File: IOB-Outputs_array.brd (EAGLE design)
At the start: 106.7 x 104.1 mm, 112 parts

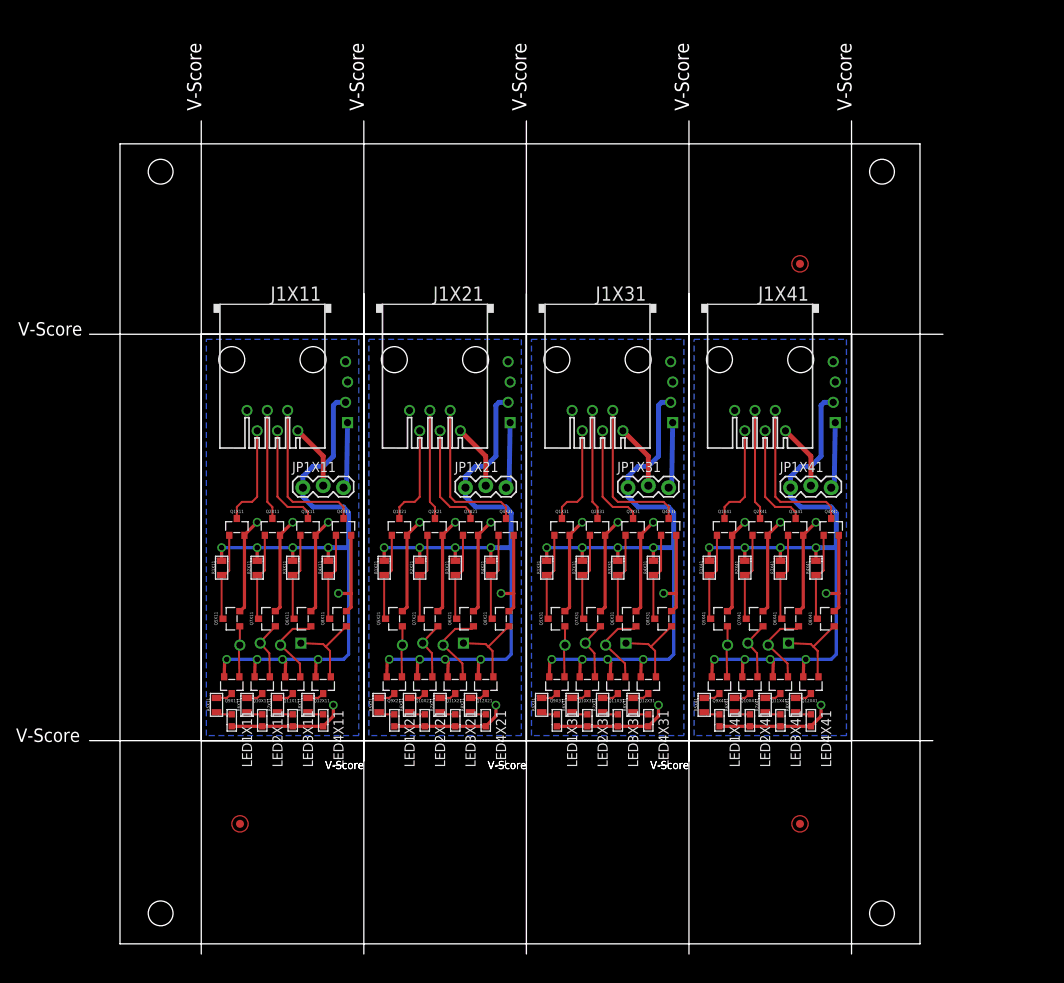
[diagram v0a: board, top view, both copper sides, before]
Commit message: updated to new IOB design
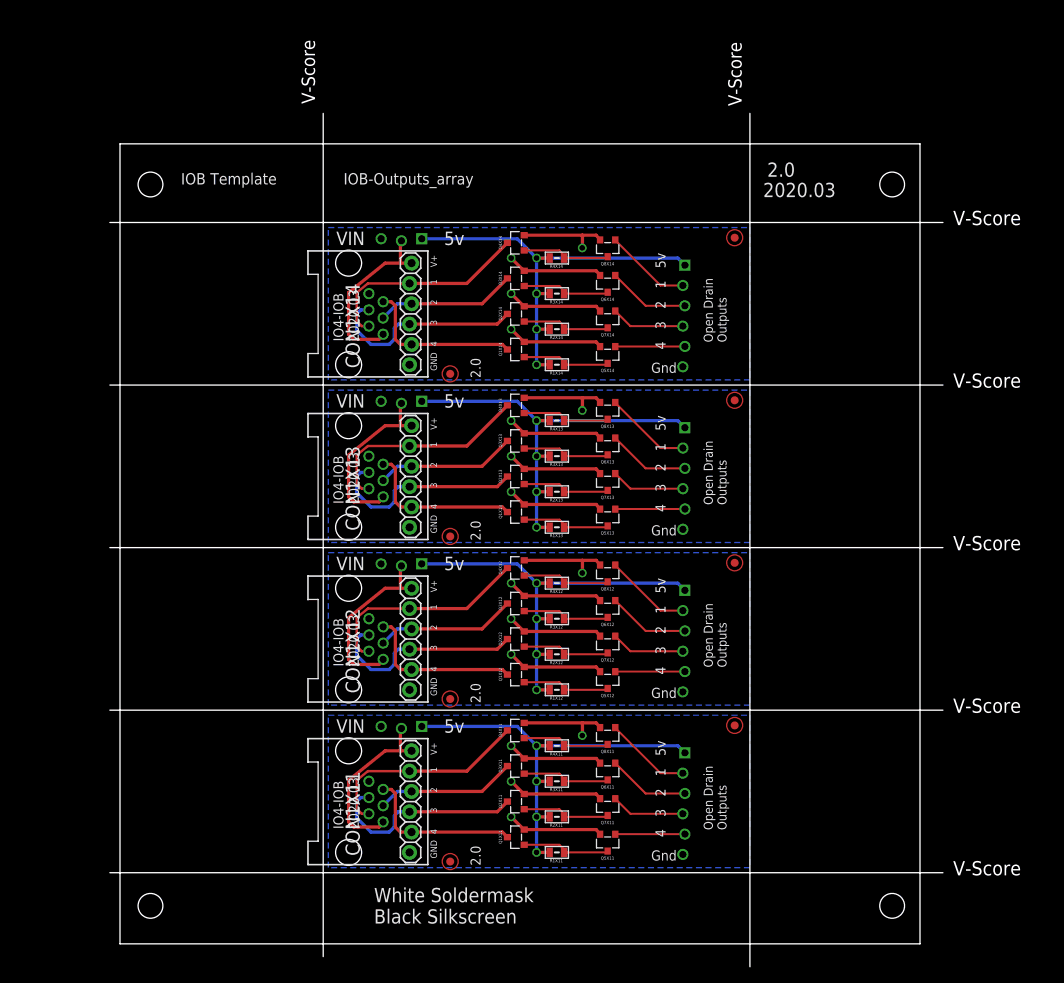
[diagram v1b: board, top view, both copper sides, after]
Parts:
- removed IOBX11, IOBX21, IOBX31, IOBX41: (no value), SPCoast:IO4-IOB
- removed J1X11, J1X21, J1X31, J1X41: (no value), SPCoast:RJ25-PANEL
- removed JP1X11, JP1X21, JP1X31, JP1X41: (no value), SPCoast:1X03
- removed LED1X11, LED1X21, LED1X31, LED1X41, LED2X11, LED2X21, LED2X31, LED2X41, LED3X11, LED3X21, LED3X31, LED3X41, LED4X11, LED4X21, LED4X31, LED4X41: (no value), SPCoast:0603-LED
- removed Q10X11, Q10X21, Q10X31, Q10X41, Q11X11, Q11X21, Q11X31, Q11X41, Q12X11, Q12X21, Q12X31, Q12X41, Q1X21, Q1X31, Q1X41, Q2X21, Q2X31, Q2X41, Q3X21, Q3X31, Q3X41, Q4X21, Q4X31, Q4X41, Q5X21, Q5X31, Q5X41, Q6X21, Q6X31, Q6X41, Q7X21, Q7X31, Q7X41, Q8X21, Q8X31, Q8X41, Q9X11, Q9X21, Q9X31, Q9X41: (no value), SPCoast:SOT23-3
- removed R1X21, R1X31, R1X41, R2X21, R2X31, R2X41, R3X21, R3X31, R3X41, R4X21, R4X31, R4X41, R5X11, R5X21, R5X31, R5X41, R6X11, R6X21, R6X31, R6X41, R7X11, R7X21, R7X31, R7X41, R8X11, R8X21, R8X31, R8X41: (no value), SPCoast:0805-RES
- removed R8X1: (no value), SPCoast:BOARD-DINRAIL-3.17IN-4X-IOB
- removed R8X2, R8X3, R8X4: (no value), SPCoast:FIDUCIAL_1MM
- added CON1X11, CON1X12, CON1X13, CON1X14: (no value), SPCoast:RJ24-INVERTED-PINS
- added FID1X11, FID1X12, FID1X13, FID1X14, FID2X11, FID2X12, FID2X13, FID2X14: (no value), SPCoast:FIDUCIAL_1MM
- added Q1X12, Q1X13, Q1X14, Q2X12, Q2X13, Q2X14, Q3X12, Q3X13, Q3X14, Q4X12, Q4X13, Q4X14, Q5X12, Q5X13, Q5X14, Q6X12, Q6X13, Q6X14, Q7X12, Q7X13, Q7X14, Q8X12, Q8X13, Q8X14: (no value), SPCoast:SOT23-3
- added R1X12, R1X13, R1X14, R2X12, R2X13, R2X14, R3X12, R3X13, R3X14, R4X12, R4X13, R4X14: (no value), SPCoast:0805-RES
- added U$1X1: (no value), SPCoast:BOARD-DINRAIL-3.17IN-H4X-IOB
- added U$1X11, U$1X12, U$1X13, U$1X14: (no value), SPCoast:IO4-IOB
- moved R1X11 55.0 mm to (54.6, 11.4), turned to 180 degrees
- moved Q5X11 54.7 mm to (61.0, 12.7), turned to 180 degrees
- moved Q1X11 52.2 mm to (49.5, 13.3), turned to 90 degrees
- moved R2X11 48.7 mm to (54.6, 15.9), turned to 180 degrees
- moved Q7X11 48.6 mm to (61.0, 17.1), turned to 180 degrees
- moved Q2X11 45.9 mm to (49.5, 17.8), turned to 90 degrees
- moved Q6X11 42.6 mm to (61.0, 21.6), turned to 180 degrees
- moved R3X11 42.4 mm to (54.6, 20.3), turned to 180 degrees
- moved Q3X11 39.6 mm to (49.5, 22.2), turned to 90 degrees
- moved Q8X11 36.7 mm to (61.0, 26.0), turned to 180 degrees
- moved R4X11 36.2 mm to (54.6, 24.8), turned to 180 degrees
- moved Q4X11 33.3 mm to (49.5, 26.7), turned to 90 degrees
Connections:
- removed net GNDX21: IOBX21.G@1, IOBX21.G@2, J1X21.6, LED1X21.C, LED2X21.C, LED3X21.C, LED4X21.C, Q1X21.2, Q2X21.2, Q3X21.2, Q4X21.2, Q5X21.2, Q6X21.2, Q7X21.2, Q8X21.2
- removed net GNDX31: IOBX31.G@1, IOBX31.G@2, J1X31.6, LED1X31.C, LED2X31.C, LED3X31.C, LED4X31.C, Q1X31.2, Q2X31.2, Q3X31.2, Q4X31.2, Q5X31.2, Q6X31.2, Q7X31.2, Q8X31.2
- removed net GNDX41: IOBX41.G@1, IOBX41.G@2, J1X41.6, LED1X41.C, LED2X41.C, LED3X41.C, LED4X41.C, Q1X41.2, Q2X41.2, Q3X41.2, Q4X41.2, Q5X41.2, Q6X41.2, Q7X41.2, Q8X41.2
- removed net IO1X21: J1X21.2, Q4X21.3
- removed net IO1X31: J1X31.2, Q4X31.3
- removed net IO1X41: J1X41.2, Q4X41.3
- removed net IO2X21: J1X21.3, Q3X21.3
- removed net IO2X31: J1X31.3, Q3X31.3
- removed net IO2X41: J1X41.3, Q3X41.3
- removed net IO3X21: J1X21.4, Q2X21.3
- removed net IO3X31: J1X31.4, Q2X31.3
- removed net IO3X41: J1X41.4, Q2X41.3
- removed net IO4X21: J1X21.5, Q1X21.3
- removed net IO4X31: J1X31.5, Q1X31.3
- removed net IO4X41: J1X41.5, Q1X41.3
- removed net N$11X11: Q12X11.3, R8X11.2
- removed net N$11X21: Q12X21.3, R8X21.2
- removed net N$11X31: Q12X31.3, R8X31.2
- removed net N$11X41: Q12X41.3, R8X41.2
- removed net N$1X21: Q4X21.1, Q8X21.3, R4X21.1
- removed net N$1X31: Q4X31.1, Q8X31.3, R4X31.1
- removed net N$1X41: Q4X41.1, Q8X41.3, R4X41.1
- removed net N$2X11: LED4X11.A, R8X11.1
- removed net N$2X21: LED4X21.A, R8X21.1
- removed net N$2X31: LED4X31.A, R8X31.1
- removed net N$2X41: LED4X41.A, R8X41.1
- removed net N$30X11: Q11X11.3, R7X11.2
- removed net N$30X21: Q11X21.3, R7X21.2
- removed net N$30X31: Q11X31.3, R7X31.2
- removed net N$30X41: Q11X41.3, R7X41.2
- removed net N$31X11: Q10X11.3, R6X11.2
- removed net N$31X21: Q10X21.3, R6X21.2
- removed net N$31X31: Q10X31.3, R6X31.2
- removed net N$31X41: Q10X41.3, R6X41.2
- removed net N$32X11: Q9X11.3, R5X11.2
- removed net N$32X21: Q9X21.3, R5X21.2
- removed net N$32X31: Q9X31.3, R5X31.2
- removed net N$32X41: Q9X41.3, R5X41.2
- removed net N$3X11: LED3X11.A, R7X11.1
- removed net N$3X21: LED3X21.A, R7X21.1
- removed net N$3X31: LED3X31.A, R7X31.1
- removed net N$3X41: LED3X41.A, R7X41.1
- removed net N$4X11: LED2X11.A, R6X11.1
- removed net N$4X21: LED2X21.A, R6X21.1
- removed net N$4X31: LED2X31.A, R6X31.1
- removed net N$4X41: LED2X41.A, R6X41.1
- removed net N$5X11: LED1X11.A, R5X11.1
- removed net N$5X21: LED1X21.A, R5X21.1
- removed net N$5X31: LED1X31.A, R5X31.1
- removed net N$5X41: LED1X41.A, R5X41.1
- removed net N$6X21: Q3X21.1, Q6X21.3, R3X21.1
- removed net N$6X31: Q3X31.1, Q6X31.3, R3X31.1
- removed net N$6X41: Q3X41.1, Q6X41.3, R3X41.1
- removed net N$7X21: Q2X21.1, Q7X21.3, R2X21.1
- removed net N$7X31: Q2X31.1, Q7X31.3, R2X31.1
- removed net N$7X41: Q2X41.1, Q7X41.3, R2X41.1
- removed net N$8X21: Q1X21.1, Q5X21.3, R1X21.1
- removed net N$8X31: Q1X31.1, Q5X31.3, R1X31.1
- removed net N$8X41: Q1X41.1, Q5X41.3, R1X41.1
- removed net P1X21: IOBX21.P1, Q12X21.1, Q8X21.1
- removed net P1X31: IOBX31.P1, Q12X31.1, Q8X31.1
- removed net P1X41: IOBX41.P1, Q12X41.1, Q8X41.1
- removed net P2X21: IOBX21.P2, Q11X21.1, Q6X21.1
- removed net P2X31: IOBX31.P2, Q11X31.1, Q6X31.1
- removed net P2X41: IOBX41.P2, Q11X41.1, Q6X41.1
- removed net P3X21: IOBX21.P3, Q10X21.1, Q7X21.1
- removed net P3X31: IOBX31.P3, Q10X31.1, Q7X31.1
- removed net P3X41: IOBX41.P3, Q10X41.1, Q7X41.1
- removed net P4X21: IOBX21.P4, Q5X21.1, Q9X21.1
- removed net P4X31: IOBX31.P4, Q5X31.1, Q9X31.1
- removed net P4X41: IOBX41.P4, Q5X41.1, Q9X41.1
- removed net VCCIOX11: J1X11.1, JP1X11.2
- removed net VCCIOX21: J1X21.1, JP1X21.2
- removed net VCCIOX31: J1X31.1, JP1X31.2
- removed net VCCIOX41: J1X41.1, JP1X41.2
- removed net VCCX21: IOBX21.V5, JP1X21.1, Q10X21.2, Q11X21.2, Q12X21.2, Q9X21.2, R1X21.2, R2X21.2, R3X21.2, R4X21.2
- removed net VCCX31: IOBX31.V5, JP1X31.1, Q10X31.2, Q11X31.2, Q12X31.2, Q9X31.2, R1X31.2, R2X31.2, R3X31.2, R4X31.2
- removed net VCCX41: IOBX41.V5, JP1X41.1, Q10X41.2, Q11X41.2, Q12X41.2, Q9X41.2, R1X41.2, R2X41.2, R3X41.2, R4X41.2
- removed net VINX21: IOBX21.V+, JP1X21.3
- removed net VINX31: IOBX31.V+, JP1X31.3
- removed net VINX41: IOBX41.V+, JP1X41.3
- new net GNDX12: CON1X12.6, CON1X12.6@1, Q1X12.2, Q2X12.2, Q3X12.2, Q4X12.2, Q5X12.2, Q6X12.2, Q7X12.2, Q8X12.2, U$1X12.G@3
- new net GNDX13: CON1X13.6, CON1X13.6@1, Q1X13.2, Q2X13.2, Q3X13.2, Q4X13.2, Q5X13.2, Q6X13.2, Q7X13.2, Q8X13.2, U$1X13.G@3
- new net GNDX14: CON1X14.6, CON1X14.6@1, Q1X14.2, Q2X14.2, Q3X14.2, Q4X14.2, Q5X14.2, Q6X14.2, Q7X14.2, Q8X14.2, U$1X14.G@3
- new net IO1X12: CON1X12.2, CON1X12.2@1, Q4X12.3
- new net IO1X13: CON1X13.2, CON1X13.2@1, Q4X13.3
- new net IO1X14: CON1X14.2, CON1X14.2@1, Q4X14.3
- new net IO2X12: CON1X12.3, CON1X12.3@1, Q3X12.3
- new net IO2X13: CON1X13.3, CON1X13.3@1, Q3X13.3
- new net IO2X14: CON1X14.3, CON1X14.3@1, Q3X14.3
- new net IO3X12: CON1X12.4, CON1X12.4@1, Q2X12.3
- new net IO3X13: CON1X13.4, CON1X13.4@1, Q2X13.3
- new net IO3X14: CON1X14.4, CON1X14.4@1, Q2X14.3
- new net IO4X12: CON1X12.5, CON1X12.5@1, Q1X12.3
- new net IO4X13: CON1X13.5, CON1X13.5@1, Q1X13.3
- new net IO4X14: CON1X14.5, CON1X14.5@1, Q1X14.3
- new net N$1X12: Q4X12.1, Q8X12.3, R4X12.1
- new net N$1X13: Q4X13.1, Q8X13.3, R4X13.1
- new net N$1X14: Q4X14.1, Q8X14.3, R4X14.1
- new net N$6X12: Q3X12.1, Q6X12.3, R3X12.1
- new net N$6X13: Q3X13.1, Q6X13.3, R3X13.1
- new net N$6X14: Q3X14.1, Q6X14.3, R3X14.1
- new net N$7X12: Q2X12.1, Q7X12.3, R2X12.1
- new net N$7X13: Q2X13.1, Q7X13.3, R2X13.1
- new net N$7X14: Q2X14.1, Q7X14.3, R2X14.1
- new net N$8X12: Q1X12.1, Q5X12.3, R1X12.1
- new net N$8X13: Q1X13.1, Q5X13.3, R1X13.1
- new net N$8X14: Q1X14.1, Q5X14.3, R1X14.1
- new net P1X12: Q8X12.1, U$1X12.P1
- new net P1X13: Q8X13.1, U$1X13.P1
- new net P1X14: Q8X14.1, U$1X14.P1
- new net P2X12: Q6X12.1, U$1X12.P2
- new net P2X13: Q6X13.1, U$1X13.P2
- new net P2X14: Q6X14.1, U$1X14.P2
- new net P3X12: Q7X12.1, U$1X12.P3
- new net P3X13: Q7X13.1, U$1X13.P3
- new net P3X14: Q7X14.1, U$1X14.P3
- new net P4X12: Q5X12.1, U$1X12.P4
- new net P4X13: Q5X13.1, U$1X13.P4
- new net P4X14: Q5X14.1, U$1X14.P4
- new net VCCX12: R1X12.2, R2X12.2, R3X12.2, R4X12.2, U$1X12.V5, U$1X12.V5@1
- new net VCCX13: R1X13.2, R2X13.2, R3X13.2, R4X13.2, U$1X13.V5, U$1X13.V5@1
- new net VCCX14: R1X14.2, R2X14.2, R3X14.2, R4X14.2, U$1X14.V5, U$1X14.V5@1
- new net VINX12: U$1X12.V+
- new net VINX13: U$1X13.V+
- new net VINX14: U$1X14.V+
- new net VOUTX11: CON1X11.1, CON1X11.1@1, U$1X11.VOUT
- new net VOUTX12: CON1X12.1, CON1X12.1@1, U$1X12.VOUT
- new net VOUTX13: CON1X13.1, CON1X13.1@1, U$1X13.VOUT
- new net VOUTX14: CON1X14.1, CON1X14.1@1, U$1X14.VOUT
- net GNDX11: now also CON1X11.6, CON1X11.6@1, U$1X11.G@3; no longer IOBX11.G@1, IOBX11.G@2, J1X11.6, LED1X11.C, LED2X11.C, LED3X11.C, LED4X11.C
- net IO1X11: now also CON1X11.2, CON1X11.2@1; no longer J1X11.2
- net IO2X11: now also CON1X11.3, CON1X11.3@1; no longer J1X11.3
- net IO3X11: now also CON1X11.4, CON1X11.4@1; no longer J1X11.4
- net IO4X11: now also CON1X11.5, CON1X11.5@1; no longer J1X11.5
- net P1X11: now also U$1X11.P1; no longer IOBX11.P1, Q12X11.1
- net P2X11: now also U$1X11.P2; no longer IOBX11.P2, Q11X11.1
- net P3X11: now also U$1X11.P3; no longer IOBX11.P3, Q10X11.1
- net P4X11: now also U$1X11.P4; no longer IOBX11.P4, Q9X11.1
- net VCCX11: now also U$1X11.V5, U$1X11.V5@1; no longer IOBX11.V5, JP1X11.1, Q10X11.2, Q11X11.2, Q12X11.2, Q9X11.2
- net VINX11: now also U$1X11.V+; no longer IOBX11.V+, JP1X11.3
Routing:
- net VCCX41: track 86.8 -> 0.00 mm, vias 8 -> 0
- net VCCX31: track 86.8 -> 0.00 mm, vias 8 -> 0
- net VCCX21: track 86.8 -> 0.00 mm, vias 8 -> 0
- net GNDX31: track 62.1 -> 0.00 mm, vias 5 -> 0
- net GNDX21: track 62.1 -> 0.00 mm, vias 5 -> 0
- net GNDX41: track 62.1 -> 0.00 mm, vias 5 -> 0
- net VCCX12: track 0.00 -> 54.2 mm, vias 0 -> 4
- net VCCX14: track 0.00 -> 54.2 mm, vias 0 -> 4
- net VCCX13: track 0.00 -> 54.2 mm, vias 0 -> 4
- net GNDX13: track 0.00 -> 47.5 mm, vias 0 -> 4
- net GNDX12: track 0.00 -> 47.5 mm, vias 0 -> 4
- net GNDX14: track 0.00 -> 47.5 mm, vias 0 -> 4
- net VCCX11: track 86.8 -> 54.2 mm, vias 8 -> 4
- net IO1X14: track 0.00 -> 26.7 mm
- net IO1X13: track 0.00 -> 26.7 mm
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- added copper zone on layer 16, net GNDX12
- added copper zone on layer 16, net GNDX13
- added copper zone on layer 16, net GNDX14
- removed copper zone on layer 16, net GNDX21
- removed copper zone on layer 16, net GNDX31
- removed copper zone on layer 16, net GNDX41
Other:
- board size 106.7 x 104.1 mm -> 104.1 x 106.7 mm
- board text added: "2020.03"
- board text added: "CON1"
- board text added: "White Soldermask Black Silkscreen"
- board text removed: "(15,15)"
- board text removed: "(15,85)"
- board text removed: "(85,85)"
- board text removed: "1"
- board text removed: "2"
- board text removed: "2019-11"
- board text removed: "3"
- board text removed: "4"
- board text removed: "5V"
- board text removed: "5v"
- board text removed: "IO Interface"
- board text removed: "IO4 Power"
- board text removed: "J1"
- board text removed: "JP1"
- board text removed: "Made in the PCR, Coast Div, NMRA"
- board text removed: "Model Railroading is Fun!"
- board text removed: "P1"
- board text removed: "P2"
- board text removed: "P3"
- board text removed: "P4"
- board text removed: "Q10"
- board text removed: "Q11"
- board text removed: "Q12"
- board text removed: "Q9"
- board text removed: "Quad OpenDrain Output"
- board text removed: "R5"
- board text removed: "R6"
- board text removed: "R7"
- board text removed: "R8"
- board text removed: "V-Score"
- board text removed: "V2.0"
- board text removed: "VIN"
- board text removed: "Vin"
- board text removed: "White Soldermask, Black Silkscreen"

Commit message: bump version
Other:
- board text added: "3.0"
- board text added: "v3.0"
- board text removed: "2.0"
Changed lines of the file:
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@@
 <plain>
 <text x="27.94" y="14.351" size="1.27" layer="21" font="vector" rot="R90">IO4-IOB</text>
-<text x="45.085" y="9.779" size="1.27" layer="21" font="vector" rot="R90">2.0</text>
+<text x="45.085" y="9.779" size="1.27" layer="21" font="vector" rot="R90">3.0</text>
 <text x="75.819" y="14.224" size="1.143" layer="21" font="vector" rot="R90">Open Drain
 Outputs</text>
@@
 <text x="55.626" y="26.9875" size="1.016" layer="125" font="vector" rot="R180">R4</text>
 <text x="27.94" y="34.671" size="1.27" layer="21" font="vector" rot="R90">IO4-IOB</text>
-<text x="45.085" y="30.099" size="1.27" layer="21" font="vector" rot="R90">2.0</text>
+<text x="45.085" y="30.099" size="1.27" layer="21" font="vector" rot="R90">3.0</text>
 <text x="75.819" y="34.544" size="1.143" layer="21" font="vector" rot="R90">Open Drain
 Outputs</text>
@@
 <text x="55.626" y="47.3075" size="1.016" layer="125" font="vector" rot="R180">R4</text>
 <text x="27.94" y="54.991" size="1.27" layer="21" font="vector" rot="R90">IO4-IOB</text>
-<text x="45.085" y="50.419" size="1.27" layer="21" font="vector" rot="R90">2.0</text>
+<text x="45.085" y="50.419" size="1.27" layer="21" font="vector" rot="R90">3.0</text>
 <text x="75.819" y="54.864" size="1.143" layer="21" font="vector" rot="R90">Open Drain
 Outputs</text>
@@
 <text x="55.626" y="67.6275" size="1.016" layer="125" font="vector" rot="R180">R4</text>
 <text x="27.94" y="75.311" size="1.27" layer="21" font="vector" rot="R90">IO4-IOB</text>
-<text x="45.085" y="70.739" size="1.27" layer="21" font="vector" rot="R90">2.0</text>
+<text x="45.085" y="70.739" size="1.27" layer="21" font="vector" rot="R90">3.0</text>
 <text x="75.819" y="75.184" size="1.143" layer="21" font="vector" rot="R90">Open Drain
 Outputs</text>
@@
 <text x="55.626" y="83.6295" size="1.016" layer="125" font="vector" rot="R180">R3</text>
 <text x="55.626" y="87.9475" size="1.016" layer="125" font="vector" rot="R180">R4</text>
-<text x="80.391" y="93.345" size="1.778" layer="21" font="vector">2020.03</text>
-<text x="80.899" y="95.885" size="1.778" layer="21" font="vector">2.0</text>
+<text x="80.391" y="92.71" size="1.778" layer="21" font="vector">2020.03</text>
+<text x="80.899" y="95.885" size="1.778" layer="21" font="vector">v3.0</text>
 </plain>
 <attributes>
